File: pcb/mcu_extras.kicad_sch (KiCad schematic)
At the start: 9 parts, among them J1 UART

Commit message: Finished schematic
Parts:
- removed JP2: EN-SW, Jumper:SolderJumper-2_P1.3mm_Bridged_RoundedPad1.0x1.5mm, symbol Jumper:SolderJumper_2_Bridged
- removed JP3: IO9, symbol Jumper:SolderJumper_2_Open
- removed R1, R3: 10kR, symbol Device:R
- C15: renamed from C3; footprint (none) -> Capacitor_SMD:C_0603_1608Metric; LCSC Part (none) -> C19702
- C16: renamed from C4; value C -> 100nF; footprint (none) -> Capacitor_SMD:C_0603_1608Metric; LCSC Part (none) -> C14663
- R13: renamed from R2; footprint (none) -> Resistor_SMD:R_0603_1608Metric; LCSC Part (none) -> C2930027
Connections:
- net EN: now also C16.2, JP1.2 (B)

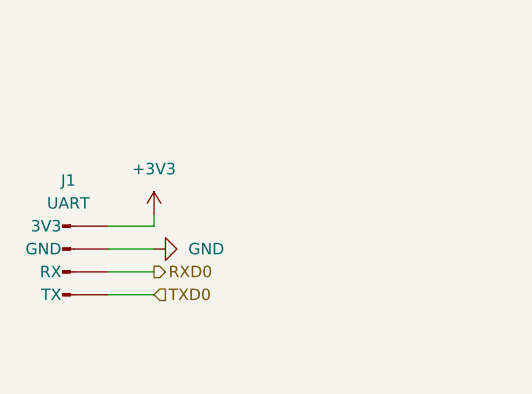
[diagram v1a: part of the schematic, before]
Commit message: Finished routing and added silkscreen art
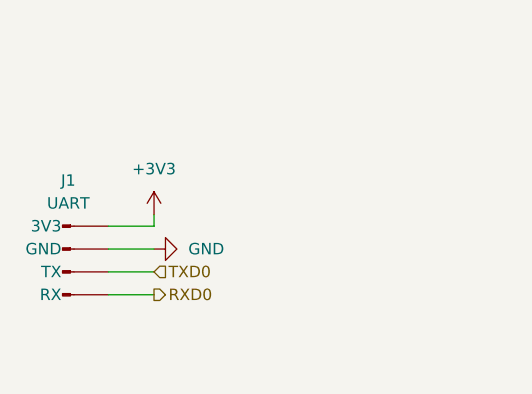
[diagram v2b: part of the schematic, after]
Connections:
- net RXD0: now also J1.4 (RX); no longer J1.3 (RX)
- net TXD0: now also J1.3 (TX); no longer J1.4 (TX)
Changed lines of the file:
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@@
-	(wire
-		(pts
-			(xy 44.45 90.17) (xy 49.53 90.17)
-		)
-		(stroke
-			(width 0)
-			(type default)
-		)
-	)
 	(wire
 		(pts
@@
 	(wire
 		(pts
-			(xy 44.45 87.63) (xy 49.53 87.63)
-		)
-		(stroke
-			(width 0)
-			(type default)
-		)
-	)
-	(wire
-		(pts
 			(xy 123.19 78.74) (xy 119.38 78.74)
 		)
@@
 	(wire
 		(pts
+			(xy 44.45 90.17) (xy 49.53 90.17)
+		)
+		(stroke
+			(width 0)
+			(type default)
+		)
+	)
+	(wire
+		(pts
+			(xy 44.45 87.63) (xy 49.53 87.63)
+		)
+		(stroke
+			(width 0)
+			(type default)
+		)
+	)
+	(wire
+		(pts
 			(xy 49.53 81.28) (xy 49.53 82.55)
 		)
@@
 		)
 	)
-	(hierarchical_label "TXD0"
-		(shape input)
+	(hierarchical_label "RXD0"
+		(shape output)
 		(at 49.53 90.17 0)
 		(effects
@@
 		)
 	)
-	(hierarchical_label "RXD0"
-		(shape output)
+	(hierarchical_label "TXD0"
+		(shape input)
 		(at 49.53 87.63 0)
 		(effects
